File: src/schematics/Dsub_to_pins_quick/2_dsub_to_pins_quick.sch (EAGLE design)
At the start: 39 parts, among them X1 22-23-2021, X10 22-23-2021, X11 22-23-2021, X12 22-23-2021, X13 22-23-2021, X14 22-23-2021, X15 22-23-2021, X16 22-23-2021, X17 22-23-2021, X18 22-23-2021, X19 22-23-2021, X2 22-23-2021, X20 22-23-2021, X21 22-23-2021, X22 22-23-2021, X23 22-23-2021, X24 22-23-2021, X25 22-23-2021, X26 22-23-2021, X27 22-23-2021, X28 22-23-2021, X29 22-23-2021, X3 22-23-2021, X30 22-23-2021, X31 22-23-2021, X32 22-23-2021, X33 22-23-2021, X34 22-23-2021, X35 22-23-2021, X36 22-23-2021, X37 22-23-2021, X4 22-23-2021, X5 22-23-2021, X6 22-23-2021, X7 22-23-2021, X8 22-23-2021, X9 22-23-2021

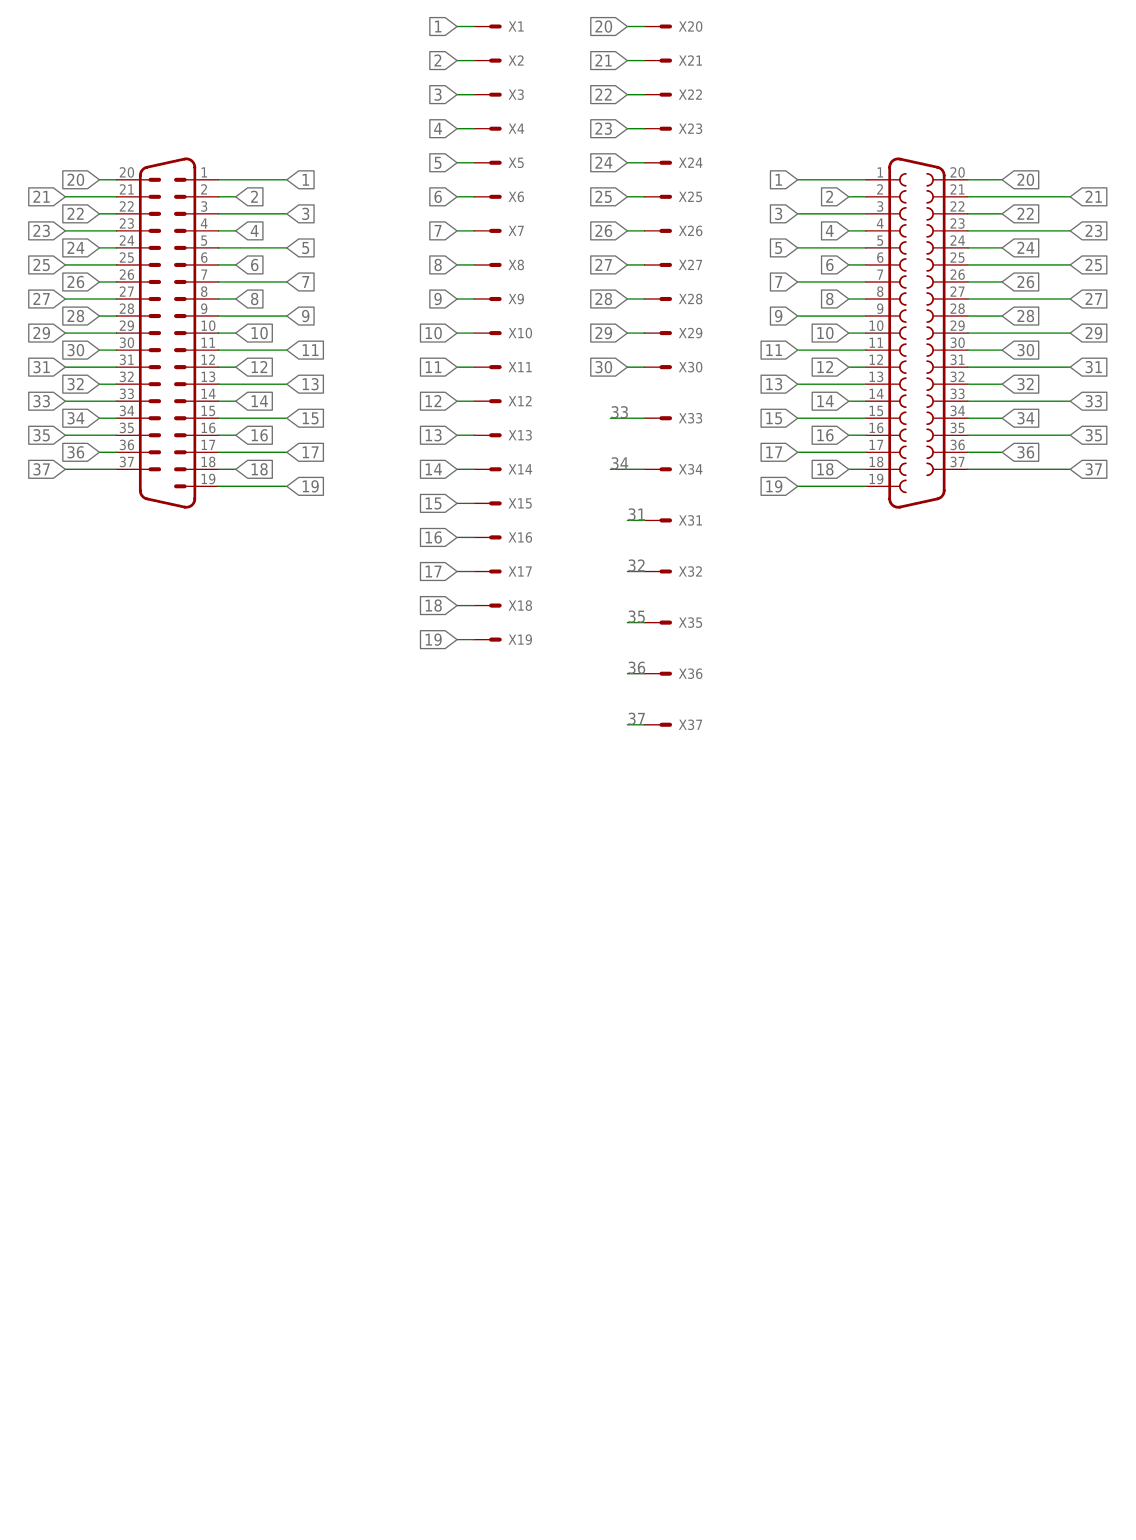
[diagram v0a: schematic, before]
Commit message: Added schematic changes from summation subtraction branch
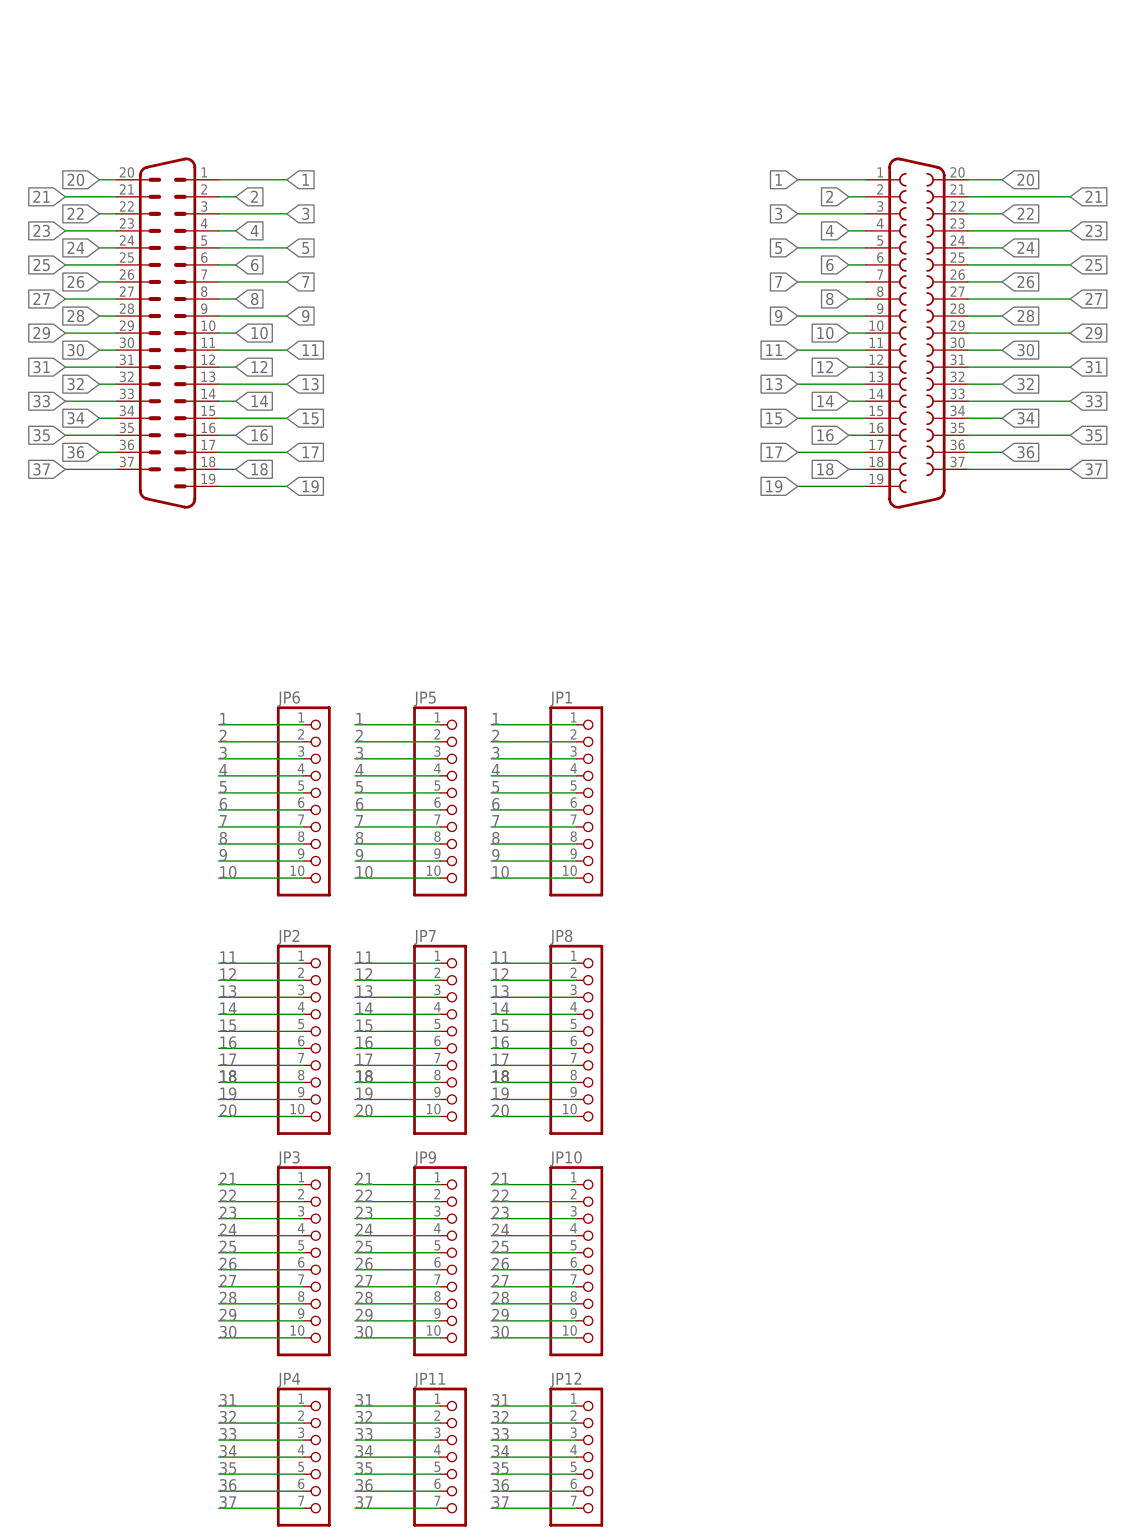
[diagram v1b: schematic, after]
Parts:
- removed X1, X10, X11, X12, X13, X14, X15, X16, X17, X18, X19, X2, X20, X21, X22, X23, X24, X25, X26, X27, X28, X29, X3, X30, X31, X32, X35, X36, X37, X4, X5, X6, X7, X8, X9: 22-23-2021, mayo:22-23-2021
- removed X40: (no value), con-subd:M37HP
- removed X41: (no value), con-subd:F37HP
- added JP1, JP10, JP2, JP3, JP5, JP6, JP7, JP8, JP9: (no value), pinhead:PINHD-1X10
- added JP11, JP12, JP4: (no value), pinhead:PINHD-1X7
- X33: value 22-23-2021 -> (none); device mayo:22-23-2021 -> con-subd:M37HP
- X34: value 22-23-2021 -> (none); device mayo:22-23-2021 -> con-subd:F37HP
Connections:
- net 1: now also JP1.1, JP5.1, JP6.1, X33.1, X34.1; no longer X1.S, X40.1, X41.1
- net 10: now also JP1.10, JP5.10, JP6.10, X33.10, X34.10; no longer X10.S, X40.10, X41.10
- net 11: now also JP2.1, JP7.1, JP8.1, X33.11, X34.11; no longer X11.S, X40.11, X41.11
- net 12: now also JP2.2, JP7.2, JP8.2, X33.12, X34.12; no longer X12.S, X40.12, X41.12
- net 13: now also JP2.3, JP7.3, JP8.3, X33.13, X34.13; no longer X13.S, X40.13, X41.13
- net 14: now also JP2.4, JP7.4, JP8.4, X33.14, X34.14; no longer X14.S, X40.14, X41.14
- net 15: now also JP2.5, JP7.5, JP8.5, X33.15, X34.15; no longer X15.S, X40.15, X41.15
- net 16: now also JP2.6, JP7.6, JP8.6, X33.16, X34.16; no longer X16.S, X40.16, X41.16
- net 17: now also JP2.7, JP7.7, JP8.7, X33.17, X34.17; no longer X17.S, X40.17, X41.17
- net 18: now also JP2.8, JP7.8, JP8.8, X33.18, X34.18; no longer X18.S, X40.18, X41.18
- net 19: now also JP2.9, JP7.9, JP8.9, X33.19, X34.19; no longer X19.S, X40.19, X41.19
- net 2: now also JP1.2, JP5.2, JP6.2, X33.2, X34.2; no longer X2.S, X40.2, X41.2
- net 20: now also JP2.10, JP7.10, JP8.10, X33.20, X34.20; no longer X20.S, X40.20, X41.20
- net 21: now also JP10.1, JP3.1, JP9.1, X33.21, X34.21; no longer X21.S, X40.21, X41.21
- net 22: now also JP10.2, JP3.2, JP9.2, X33.22, X34.22; no longer X22.S, X40.22, X41.22
- net 23: now also JP10.3, JP3.3, JP9.3, X33.23, X34.23; no longer X23.S, X40.23, X41.23
- net 24: now also JP10.4, JP3.4, JP9.4, X33.24, X34.24; no longer X24.S, X40.24, X41.24
- net 25: now also JP10.5, JP3.5, JP9.5, X33.25, X34.25; no longer X25.S, X40.25, X41.25
- net 26: now also JP10.6, JP3.6, JP9.6, X33.26, X34.26; no longer X26.S, X40.26, X41.26
- net 27: now also JP10.7, JP3.7, JP9.7, X33.27, X34.27; no longer X27.S, X40.27, X41.27
- net 28: now also JP10.8, JP3.8, JP9.8, X33.28, X34.28; no longer X28.S, X40.28, X41.28
- net 29: now also JP10.9, JP3.9, JP9.9, X33.29, X34.29; no longer X29.S, X40.29, X41.29
- net 3: now also JP1.3, JP5.3, JP6.3, X33.3, X34.3; no longer X3.S, X40.3, X41.3
- net 30: now also JP10.10, JP3.10, JP9.10, X33.30, X34.30; no longer X30.S, X40.30, X41.30
- net 31: now also JP11.1, JP12.1, JP4.1, X33.31, X34.31; no longer X31.S, X40.31, X41.31
- net 32: now also JP11.2, JP12.2, JP4.2, X33.32, X34.32; no longer X32.S, X40.32, X41.32
- net 33: now also JP11.3, JP12.3, JP4.3, X33.33, X34.33; no longer X33.S, X40.33, X41.33
- net 34: now also JP11.4, JP12.4, JP4.4, X33.34, X34.34; no longer X34.S, X40.34, X41.34
- net 35: now also JP11.5, JP12.5, JP4.5, X33.35, X34.35; no longer X35.S, X40.35, X41.35
- net 36: now also JP11.6, JP12.6, JP4.6, X33.36, X34.36; no longer X36.S, X40.36, X41.36
- net 37: now also JP11.7, JP12.7, JP4.7, X33.37, X34.37; no longer X37.S, X40.37, X41.37
- net 4: now also JP1.4, JP5.4, JP6.4, X33.4, X34.4; no longer X4.S, X40.4, X41.4
- net 5: now also JP1.5, JP5.5, JP6.5, X33.5, X34.5; no longer X40.5, X41.5, X5.S
- net 6: now also JP1.6, JP5.6, JP6.6, X33.6, X34.6; no longer X40.6, X41.6, X6.S
- net 7: now also JP1.7, JP5.7, JP6.7, X33.7, X34.7; no longer X40.7, X41.7, X7.S
- net 8: now also JP1.8, JP5.8, JP6.8, X33.8, X34.8; no longer X40.8, X41.8, X8.S
- net 9: now also JP1.9, JP5.9, JP6.9, X33.9, X34.9; no longer X40.9, X41.9, X9.S
